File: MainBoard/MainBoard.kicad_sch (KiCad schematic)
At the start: 51 parts, among them J1 1761681-3, J2 Non-Inverting Input, J3 Inverting Input, J4 Output, J5 InvertedOutput, Q1 BC557, Q10 BC557, Q11 BC557, Q12 BC547, Q13 BC557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

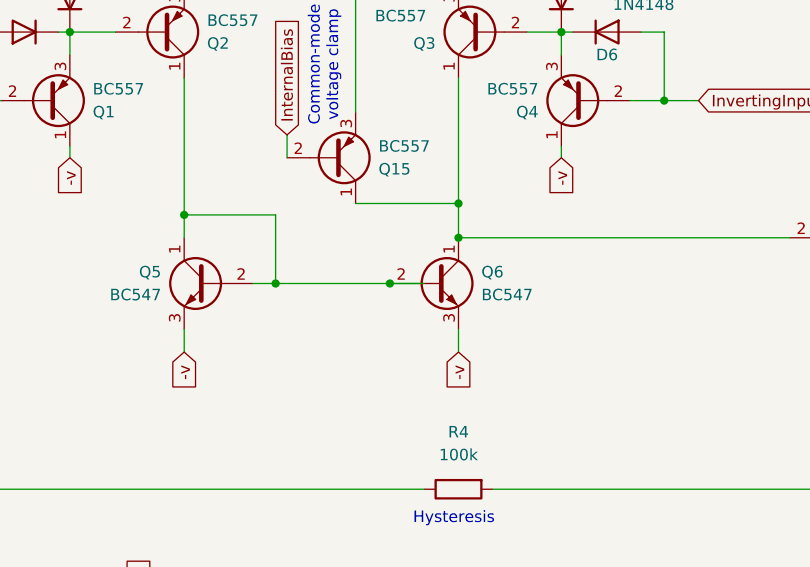
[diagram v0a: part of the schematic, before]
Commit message: added footprints
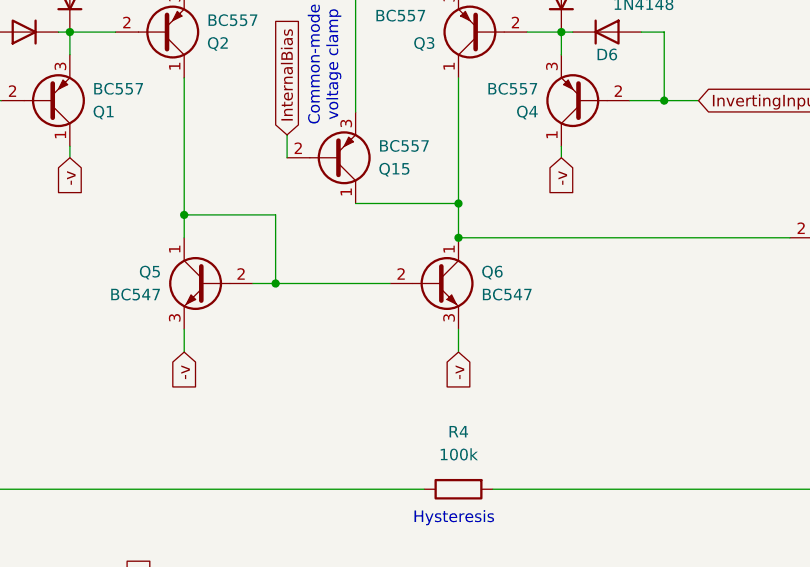
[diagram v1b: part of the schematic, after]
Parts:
- C5: footprint (none) -> Capacitor_THT:C_Rect_L9.0mm_W2.5mm_P7.50mm_MKT
- D1, D2: footprint Diode_THT:D_DO-201_P15.24mm_Horizontal -> Diode_THT:D_DO-35_SOD27_P7.62mm_Horizontal
- D10, D11, D12, D13, D14, D7, D8, D9: footprint (none) -> Diode_THT:D_DO-35_SOD27_P7.62mm_Horizontal
- J2, J3, J4, J5: footprint THONK_PJ398SM-12 -> Connector_Audio:Jack_3.5mm_QingPu_WQP-PJ398SM_Vertical_CircularHoles
- R1, R3, R4: footprint Resistor_THT:R_Axial_DIN0309_L9.0mm_D3.2mm_P2.54mm_Vertical -> Resistor_THT:R_Axial_DIN0207_L6.3mm_D2.5mm_P7.62mm_Horizontal
- RV1, RV2: footprint (none) -> Potentiometer_THT:Potentiometer_TT_P0915N
- V5: now left out of the parts list
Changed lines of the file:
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@@
 		(color 0 0 0 0)
 	)
-	(junction
-		(at 132.08 90.17)
-		(diameter 0)
-		(color 0 0 0 0)
-	)
 	(wire
 		(pts
@@
 	(wire
 		(pts
-			(xy 132.08 90.17) (xy 135.89 90.17)
-		)
-		(stroke
-			(width 0)
-			(type default)
-		)
-	)
-	(wire
-		(pts
 			(xy 96.52 22.86) (xy 96.52 39.37)
 		)
@@
 			)
 		)
-		(property "Footprint" "Resistor_THT:R_Axial_DIN0309_L9.0mm_D3.2mm_P2.54mm_Vertical"
+		(property "Footprint" "Resistor_THT:R_Axial_DIN0207_L6.3mm_D2.5mm_P7.62mm_Horizontal"
 			(at 226.568 102.87 90)
 			(effects
@@
 			)
 		)
-		(property "Footprint" ""
+		(property "Footprint" "Diode_THT:D_DO-35_SOD27_P7.62mm_Horizontal"
 			(at 104.14 140.97 0)
 			(effects
@@
 			)
 		)
-		(property "Footprint" "Diode_THT:D_DO-201_P15.24mm_Horizontal"
+		(property "Footprint" "Diode_THT:D_DO-35_SOD27_P7.62mm_Horizontal"
 			(at 75.565 170.18 0)
 			(effects
@@
 			)
 		)
-		(property "Footprint" ""
+		(property "Footprint" "Diode_THT:D_DO-35_SOD27_P7.62mm_Horizontal"
 			(at 57.15 130.81 0)
 			(effects
@@
 			)
 		)
-		(property "Footprint" "THONK_PJ398SM-12"
+		(property "Footprint" "Connector_Audio:Jack_3.5mm_QingPu_WQP-PJ398SM_Vertical_CircularHoles"
 			(at 271.78 78.74 0)
 			(effects
@@
 			)
 		)
-		(property "Footprint" ""
+		(property "Footprint" "Diode_THT:D_DO-35_SOD27_P7.62mm_Horizontal"
 			(at 25.4 130.81 0)
 			(effects
@@
 			)
 		)
-		(property "Footprint" ""
+		(property "Footprint" "Potentiometer_THT:Potentiometer_TT_P0915N"
 			(at 275.59 38.1 0)
 			(effects
@@
 			)
 		)
-		(property "Footprint" "Resistor_THT:R_Axial_DIN0309_L9.0mm_D3.2mm_P2.54mm_Vertical"
+		(property "Footprint" "Resistor_THT:R_Axial_DIN0207_L6.3mm_D2.5mm_P7.62mm_Horizontal"
 			(at 213.868 44.45 90)
 			(effects
@@
 			)
 		)
-		(property "Footprint" ""
+		(property "Footprint" "Diode_THT:D_DO-35_SOD27_P7.62mm_Horizontal"
 			(at 83.82 140.97 0)
 			(effects
@@
 		(unit 1)
 		(exclude_from_sim no)
-		(in_bom yes)
-		(on_board yes)
+		(in_bom no)
+		(on_board no)
 		(dnp yes)
 		(property "Reference" "V5"
@@
 			)
 		)
-		(property "Footprint" "THONK_PJ398SM-12"
+		(property "Footprint" "Connector_Audio:Jack_3.5mm_QingPu_WQP-PJ398SM_Vertical_CircularHoles"
 			(at 271.78 101.6 0)
 			(effects
@@
 			)
 		)
-		(property "Footprint" ""
+		(property "Footprint" "Diode_THT:D_DO-35_SOD27_P7.62mm_Horizontal"
 			(at 25.4 140.97 0)
 			(effects
@@
 			)
 		)
-		(property "Footprint" "Diode_THT:D_DO-201_P15.24mm_Horizontal"
+		(property "Footprint" "Diode_THT:D_DO-35_SOD27_P7.62mm_Horizontal"
 			(at 75.565 180.34 0)
 			(effects
@@
 			)
 		)
-		(property "Footprint" "THONK_PJ398SM-12"
+		(property "Footprint" "Connector_Audio:Jack_3.5mm_QingPu_WQP-PJ398SM_Vertical_CircularHoles"
 			(at 271.78 25.4 0)
 			(effects
@@
 			)
 		)
-		(property "Footprint" "Resistor_THT:R_Axial_DIN0309_L9.0mm_D3.2mm_P2.54mm_Vertical"
+		(property "Footprint" "Resistor_THT:R_Axial_DIN0207_L6.3mm_D2.5mm_P7.62mm_Horizontal"
 			(at 139.7 111.252 90)
 			(effects
@@
 			)
 		)
-		(property "Footprint" ""
+		(property "Footprint" "Capacitor_THT:C_Rect_L9.0mm_W2.5mm_P7.50mm_MKT"
 			(at 213.0552 104.14 0)
 			(effects
@@
 			)
 		)
-		(property "Footprint" ""
+		(property "Footprint" "Diode_THT:D_DO-35_SOD27_P7.62mm_Horizontal"
 			(at 104.14 130.81 0)
 			(effects
@@
 			)
 		)
-		(property "Footprint" ""
+		(property "Footprint" "Diode_THT:D_DO-35_SOD27_P7.62mm_Horizontal"
 			(at 57.15 140.97 0)
 			(effects
@@
 			)
 		)
-		(property "Footprint" "THONK_PJ398SM-12"
+		(property "Footprint" "Connector_Audio:Jack_3.5mm_QingPu_WQP-PJ398SM_Vertical_CircularHoles"
 			(at 24.13 64.77 0)
 			(effects
@@
 			)
 		)
-		(property "Footprint" ""
+		(property "Footprint" "Diode_THT:D_DO-35_SOD27_P7.62mm_Horizontal"
 			(at 83.82 130.81 0)
 			(effects
@@
 			)
 		)
-		(property "Footprint" ""
+		(property "Footprint" "Potentiometer_THT:Potentiometer_TT_P0915N"
 			(at 60.96 34.29 0)
 			(effects

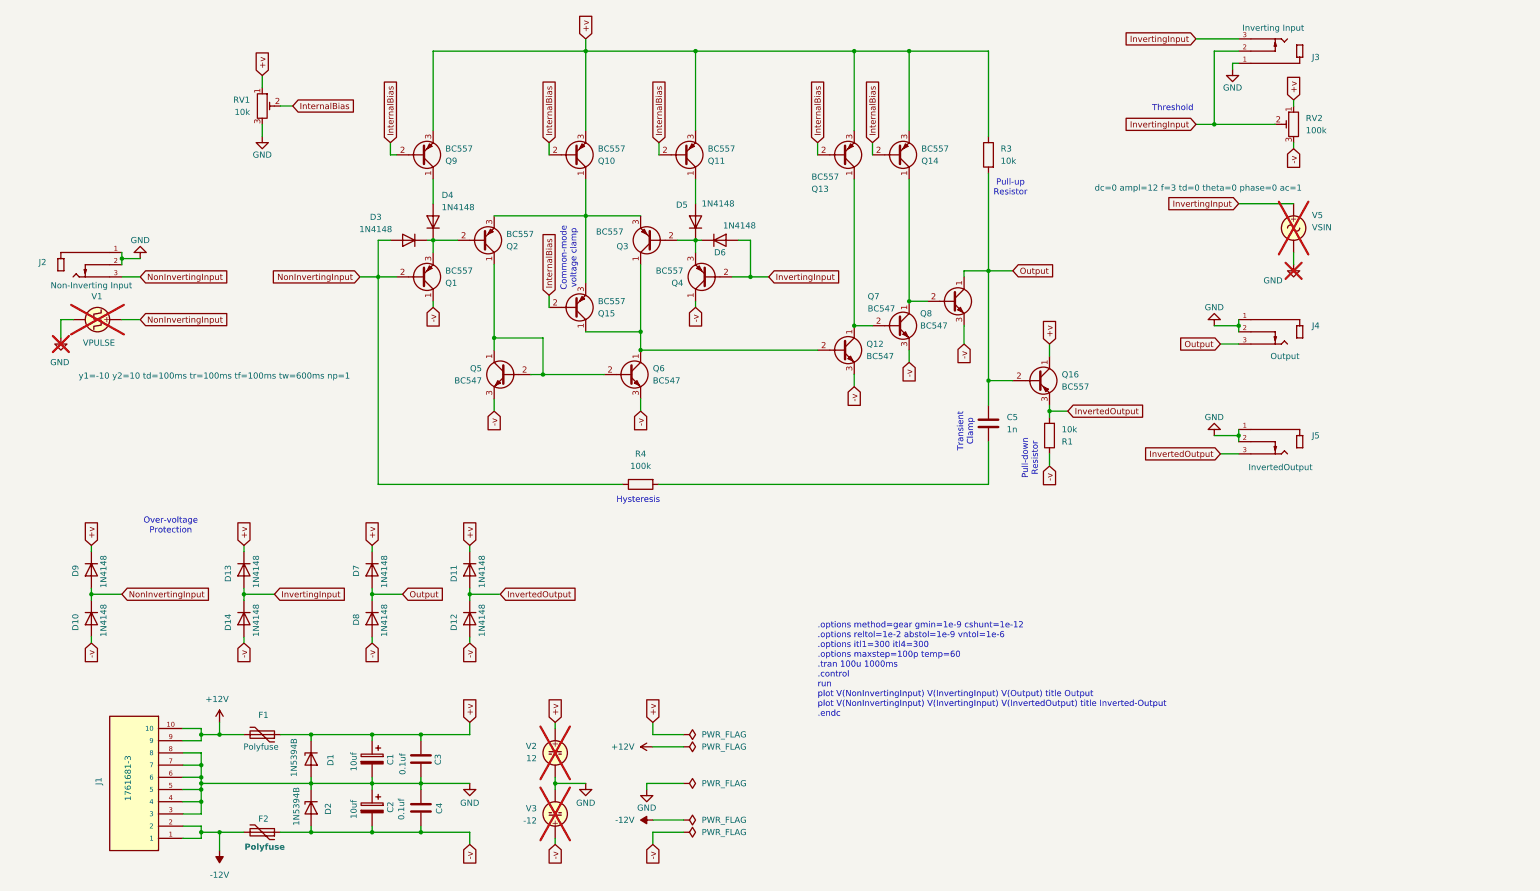
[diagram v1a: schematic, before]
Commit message: pushed comparator sub-circuit into hierarchical sheets for purposes of moving toward a window-comparator
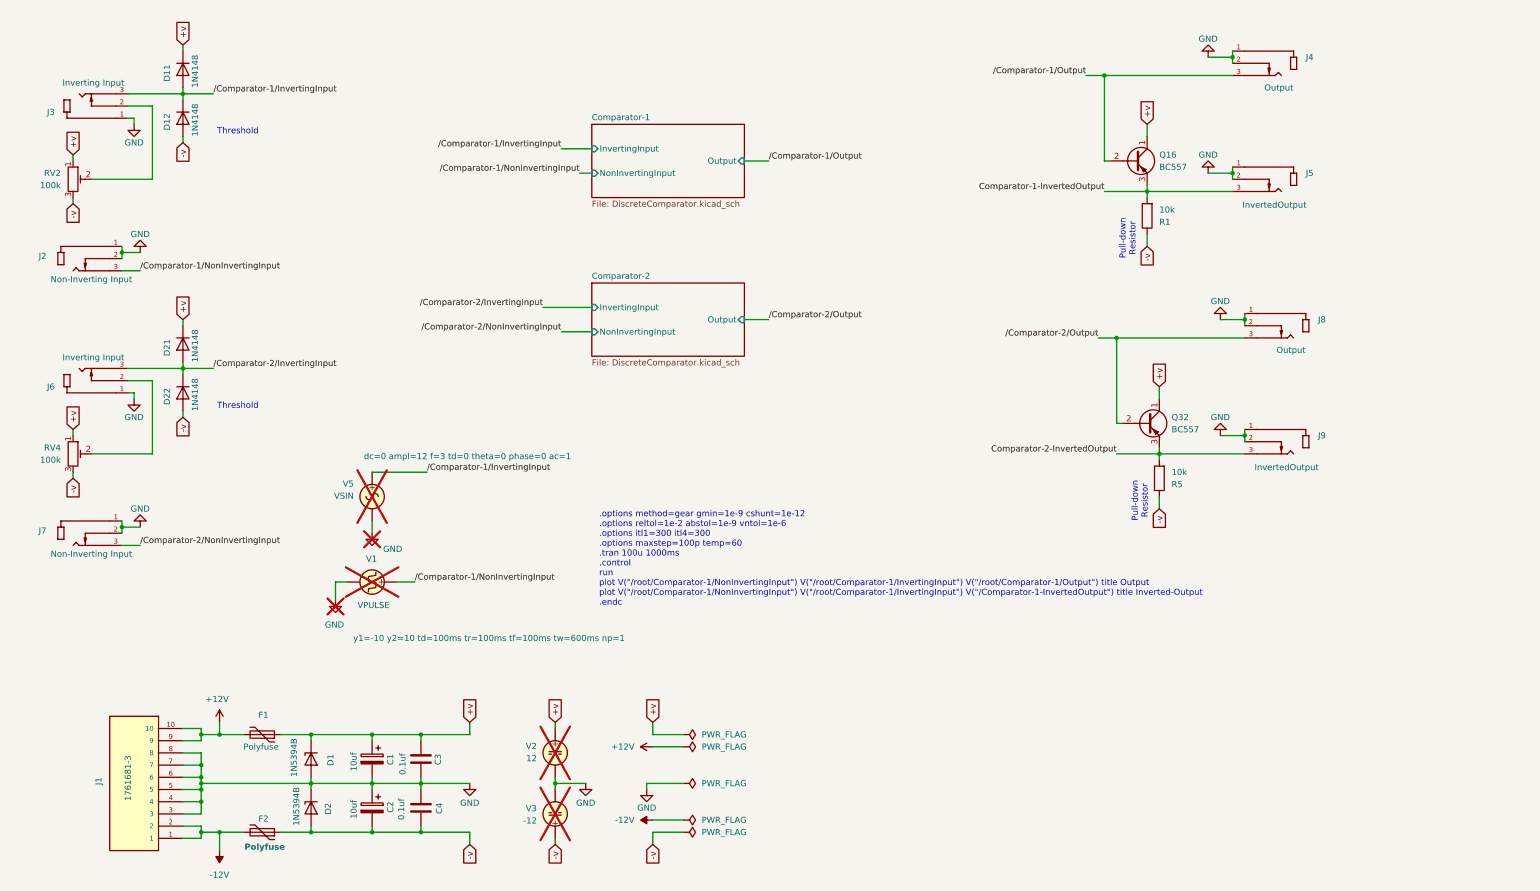
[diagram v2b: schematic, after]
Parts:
- removed C5: 1n, Capacitor_THT:C_Rect_L9.0mm_W2.5mm_P7.50mm_MKT, symbol Device:C
- removed D10, D13, D14, D7, D8, D9: 1N4148, Diode_THT:D_DO-35_SOD27_P7.62mm_Horizontal, symbol Device:D
- removed D3, D4, D5, D6: 1N4148, Diode_THT:D_DO-35_SOD27_P7.62mm_Horizontal, symbol Diode:1N4148
- removed Q1, Q10, Q11, Q13, Q14, Q15, Q2, Q3, Q4, Q9: BC557, Package_TO_SOT_THT:TO-92_Inline, symbol Transistor_BJT:BC557
- removed Q12, Q5, Q6, Q7, Q8: BC547, Package_TO_SOT_THT:TO-92_Inline, symbol Transistor_BJT:BC547
- removed R3: 10k, Resistor_THT:R_Axial_DIN0207_L6.3mm_D2.5mm_P7.62mm_Horizontal, symbol Device:R
- removed R4: 100k, Resistor_THT:R_Axial_DIN0207_L6.3mm_D2.5mm_P7.62mm_Horizontal, symbol Device:R
- removed RV1: 10k, Potentiometer_THT:Potentiometer_TT_P0915N, symbol Device:R_Potentiometer_Trim
- added D21, D22: 1N4148, Diode_THT:D_DO-35_SOD27_P7.62mm_Horizontal, symbol Device:D
- added J6: Inverting Input, Connector_Audio:Jack_3.5mm_QingPu_WQP-PJ398SM_Vertical_CircularHoles, symbol PJ398SM-12:PJ398SM-12
- added J7: Non-Inverting Input, Connector_Audio:Jack_3.5mm_QingPu_WQP-PJ398SM_Vertical_CircularHoles, symbol PJ398SM-12:PJ398SM-12
- added J8: Output, Connector_Audio:Jack_3.5mm_QingPu_WQP-PJ398SM_Vertical_CircularHoles, symbol PJ398SM-12:PJ398SM-12
- added J9: InvertedOutput, Connector_Audio:Jack_3.5mm_QingPu_WQP-PJ398SM_Vertical_CircularHoles, symbol PJ398SM-12:PJ398SM-12
- added Q32: BC557, Package_TO_SOT_THT:TO-92_Inline, symbol Transistor_BJT:BC557
- added R5: 10k, Resistor_THT:R_Axial_DIN0207_L6.3mm_D2.5mm_P7.62mm_Horizontal, symbol Device:R
- added RV4: 100k, Potentiometer_THT:Potentiometer_TT_P0915N, symbol Device:R_Potentiometer_Trim
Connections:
- net +v: now also D21.1 (K), Q32.1 (C), RV4.1
- net -v: now also D22.2 (A), R5.1, RV4.3
- net GND: now also J6.1, J7.1, J7.2, J8.1, J8.2, J9.1, J9.2
- net InvertedOutput renamed Comparator-1-InvertedOutput
- net Comparator-1-InvertedOutput: no longer D11.2 (A), D12.1 (K)
- net InvertingInput: no longer names the net of J3.2, RV2.2
- net InvertingInput: no longer J3.3, V5.1
- net NonInvertingInput renamed /Comparator-1/NonInvertingInput
- net Output renamed /Comparator-1/Output
- new net: J6.2, RV4.2
- new net Comparator-2-InvertedOutput: J9.3, Q32.3 (E), R5.2
- new net /Comparator-1/InvertingInput: D11.2 (A), D12.1 (K), J3.3, V5.1
- new net /Comparator-2/InvertingInput: D21.2 (A), D22.1 (K), J6.3
- new net /Comparator-2/NonInvertingInput: J7.3
- new net /Comparator-2/Output: J8.3, Q32.2 (B)
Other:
- added sheet Comparator-1 (DiscreteComparator.kicad_sch)
- added sheet Comparator-2 (DiscreteComparator.kicad_sch)
- note added: ".options method=gear gmin=1e-9 cshunt=1e-12 .options reltol=1e-2 abstol=1e-9 vntol=1e-6 .options itl1=300 itl4=300 .options maxstep=100p temp=60 .tran 100u 1000ms .control run plot V("/root/Comparator-1/NonInvertingInput") V("/root/Comparator-1/InvertingInput") V("/root/Comparator-1/Output") title Output plot V("/root/Comparator-1/NonInvertingInput") V("/root/Comparator-1/InvertingInput") V("/Com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"
- note removed: ".options method=gear gmin=1e-9 cshunt=1e-12 .options reltol=1e-2 abstol=1e-9 vntol=1e-6 .options itl1=300 itl4=300 .options maxstep=100p temp=60 .tran 100u 1000ms .control run plot V(NonInvertingInput) V(InvertingInput) V(Output) title Output plot V(NonInvertingInput) V(InvertingInput) V(InvertedOutput) title Inverted-Output .endc"
- note removed: "Common-mode voltage clamp"
- note removed: "Hysteresis"
- note removed: "Over-voltage Protection"
- note removed: "Pull-up Resistor"
- note removed: "Transient Clamp"
- moved on the sheet: D11, D12, J2, J3, J4, J5, Q16, R1, RV2, V1, V5

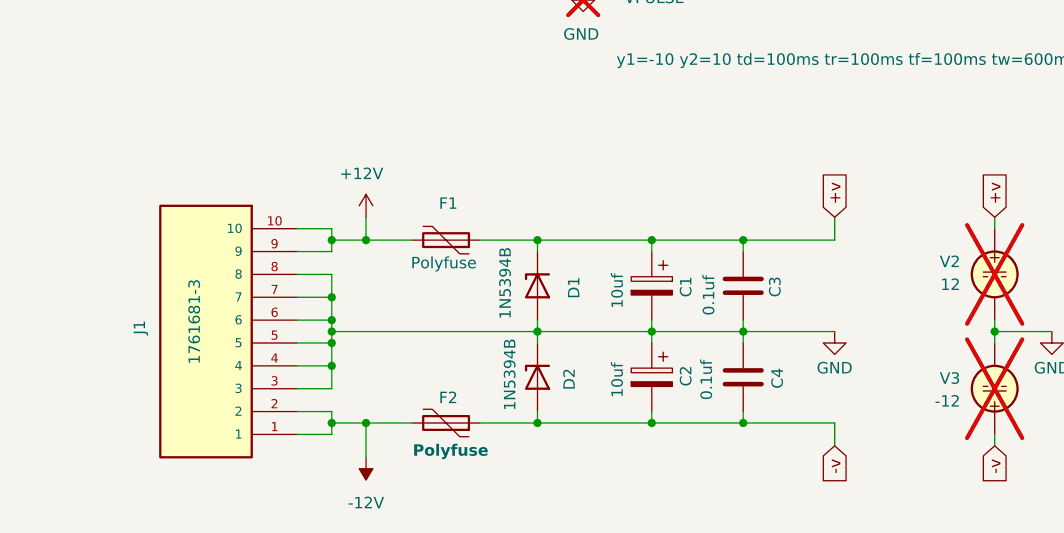
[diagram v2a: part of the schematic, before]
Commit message: added additional decoupling caps for second comparator
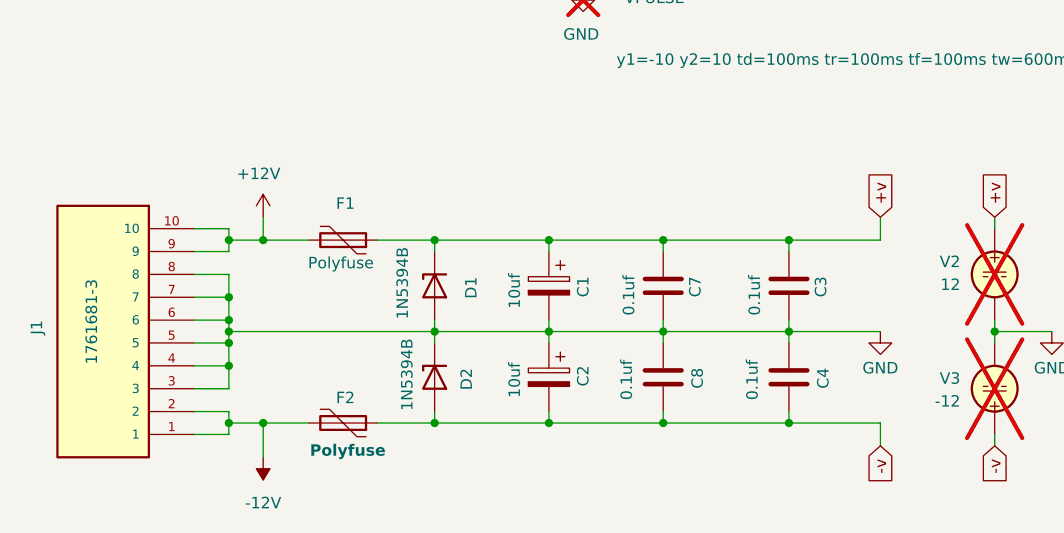
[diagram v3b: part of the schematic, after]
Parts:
- added C7, C8: 0.1uf, Capacitor_THT:C_Disc_D5.0mm_W2.5mm_P2.50mm, symbol Device:C
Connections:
- net +v: now also C7.1
- net -v: now also C8.2
- net GND: now also C7.2, C8.1
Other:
- moved on the sheet: C1, C2, C3, C4, D1, D2, F1, F2, J1
